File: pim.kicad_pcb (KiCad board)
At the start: 2 copper layers, 96.4 x 66.5 mm, 13 parts, among them J1 DE9_Plug, J2 DE9_Plug, J3 Conn_01x20_Pin, J4 Conn_01x03_MountingPin, U1 RaspberryPi_Pico_W

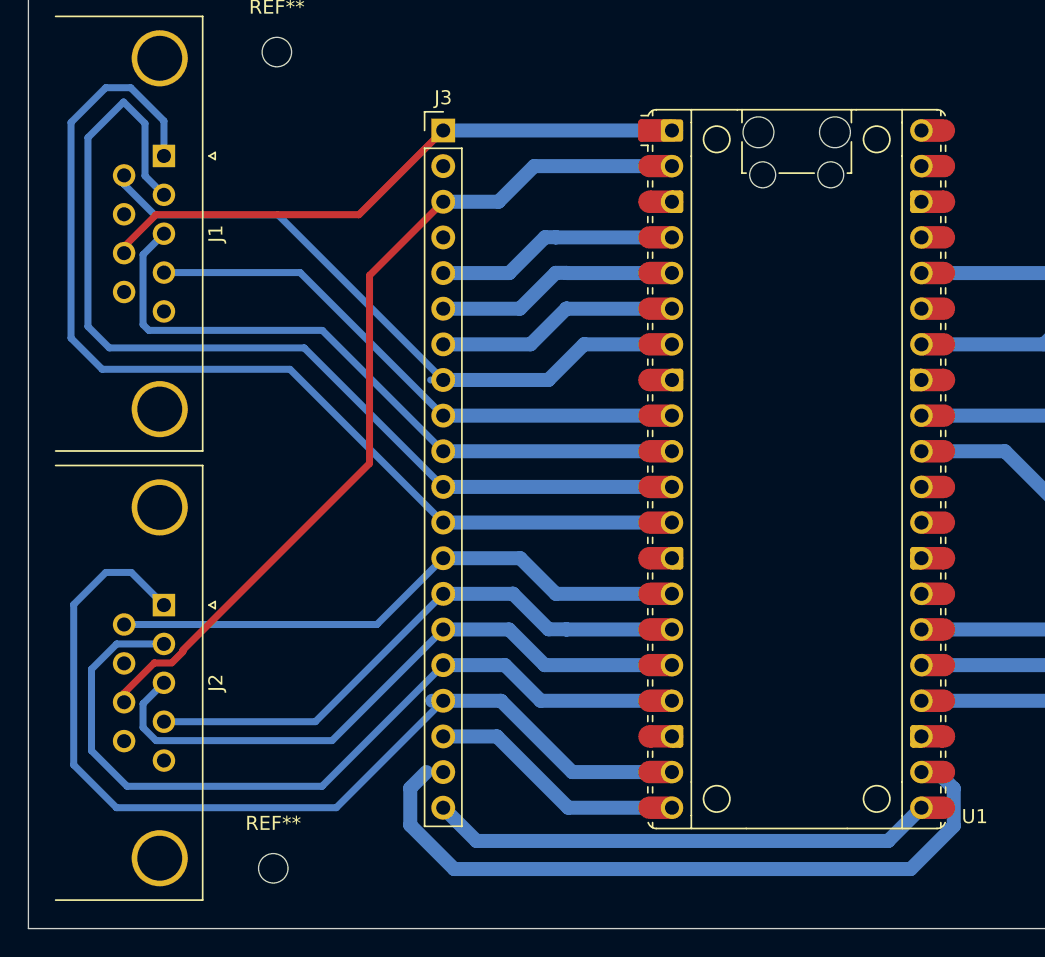
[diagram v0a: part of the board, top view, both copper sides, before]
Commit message: enlarge space between tracks
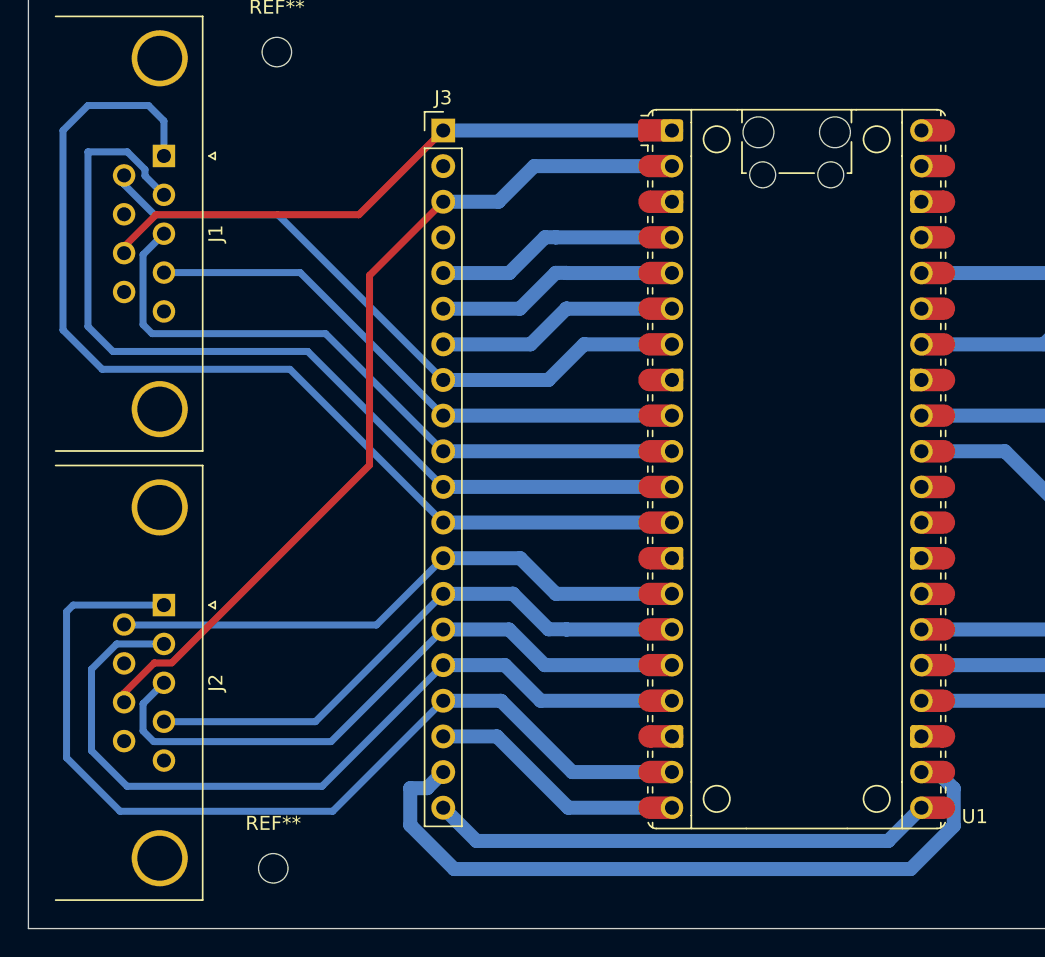
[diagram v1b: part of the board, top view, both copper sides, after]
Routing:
- net /M-1: track 71.2 -> 66.2 mm
- net /M-d: track 69.7 -> 67.6 mm
- net /M-4: track 47.4 -> 46.5 mm
- net /M-0: track 74.8 -> 74.2 mm

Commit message: WIP Working on adding support to raspberry-pi joystick connection
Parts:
- removed REF** (x4): MountingHole_2.1mm, MountingHole:MountingHole_2.1mm
- added J6: Conn_02x06_Counter_Clockwise_MountingPin, Connector_PinSocket_2.54mm:PinSocket_1x12_P2.54mm_Vertical, F.Cu at (190.8, 41.1)
- added JP1: Jumper_3_Open, Connector_PinSocket_2.54mm:PinSocket_1x03_P2.54mm_Vertical, F.Cu at (89.6, 40.9)
- added JP2: Jumper_3_Open, Connector_PinSocket_2.54mm:PinSocket_1x03_P2.54mm_Vertical, F.Cu at (102.1, 41.0)
- moved J4 63.2 mm to (171.2, 84.1)
- moved D1 63.2 mm to (171.2, 63.8)
- moved J3 63.2 mm to (108.6, 46.0)
- moved R1 63.2 mm to (152.7, 59.9)
- moved R2 63.2 mm to (152.7, 66.3)
- moved R3 63.2 mm to (152.7, 72.9)
- moved U1 63.2 mm to (133.8, 70.1)
- moved J1 52.5 mm to (77.0, 47.8)
- moved J2 52.5 mm to (77.0, 79.8)
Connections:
- J1 pad 8: /M-i -> /J1-MODE
- J2 pad 8: /M-8 -> /J2-MODE
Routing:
- net /J2-MODE: track 0.00 -> 58.9 mm
- net /M-8: track 63.2 -> 30.2 mm
- net /J1-MODE: track 0.00 -> 19.8 mm
- net /M-e: track 58.8 -> 70.6 mm
- net /M-f: track 46.4 -> 58.0 mm
- net /M-d: track 67.6 -> 79.3 mm
- net /M-1: track 66.2 -> 77.8 mm
- net /M-0: track 74.2 -> 85.8 mm
- net /M-h: track 42.1 -> 53.7 mm
- net /M-g: track 41.0 -> 52.7 mm
- net /M-4: track 46.5 -> 58.1 mm
- net /M-3: track 40.4 -> 52.0 mm
- net /M-2: track 48.5 -> 60.1 mm
- net /M-i: track 42.9 -> 44.2 mm
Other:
- board size 96.4 x 66.5 mm -> 137.3 x 66.5 mm
